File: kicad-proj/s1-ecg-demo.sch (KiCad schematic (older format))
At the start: 1 part

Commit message: added schematic
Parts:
- added C? (x2): 0.22u, symbol Device:C_Small
- added C? (x2): 0.1u, symbol Device:C_Small
- added C?: 1n, symbol Device:C_Small
- added C?: 22n, symbol Device:C_Small
- added C?: 11n, symbol Device:C_Small
- added D?: LED, symbol Device:LED
- added J?: USB-C-16-Pin, symbol s1-ecg-demo:USB-C-16-Pin
- added J?: Conn_ARM_JTAG_SWD_10, symbol Connector:Conn_ARM_JTAG_SWD_10
- added J?: Battery Port, symbol Connector_Generic:Conn_01x02
- added R? (x2): 5.1k, symbol Device:R_Small
- added R? (x2): 1M, symbol Device:R_Small
- added R? (x2): 100k, symbol Device:R_Small
- added R? (x6): 10M, symbol Device:R_Small
- added R? (x3): 150k, symbol Device:R_Small
- added R?: 665, symbol Device:R_Small
- added U?: AD8233, symbol s1-ecg-demo:AD8233
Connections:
- net GND: now reaches MOD?.1 (GND)
- net GND: now also MOD?.14 (GND), MOD?.20 (GND), C?.2, C?.2, D?.1 (K), J?.2 (Pin_2), J?.3 (GND), J?.5 (GND), J?.9 (GNDDetect), J?.A1/B12 (GND), J?.A12/B1 (GND), R?.1, R?.1, R?.2, U?.A1 (GND), U?.B3 (FR)
- net VBUS: now reaches MOD?.10 (Vcharge)
- net VBUS: now also J?.A4/B9 (VBUS), J?.A9/B4 (VBUS)
- net VBAT: now reaches MOD?.11 (Vbattery)
- net VBAT: now also J?.1 (Pin_1)
- net A3V3: now reaches MOD?.13 (Vio)
- net A3V3: now also C?.1, R?.2, U?.A2 (V+), U?.B1 (~SDN), U?.B2 (AC/~DC), U?.C2 (RLD_~SDN)
- net RA: now reaches MOD?.15 (A2)
- net RA: now also R?.1, R?.2
- net LA: now reaches MOD?.16 (A1)
- net LA: now also R?.1, R?.2
- net VREF: now reaches MOD?.17 (Vadc)
- net VREF: now also J?.1 (VTref)
- net SWDIO: now reaches MOD?.18 (SWDIO)
- net SWDIO: now also J?.2 (SWDIO/TMS)
- net SWDCLK: now reaches MOD?.19 (SWDCLK)
- net SWDCLK: now also J?.4 (SWDCLK/TCK)
- net D-: now reaches MOD?.2 (D2)
- net D-: now also J?.A7 (D-), J?.B7 (D-)
- net LED: now reaches MOD?.3 (D3)
- net LED: now also R?.2
- net LOD: now reaches MOD?.4 (D4)
- net LOD: now also U?.C1 (LOD)
- net D+: now reaches MOD?.5 (D1)
- net D+: now also J?.A6 (D+), J?.B6 (D+)
- new net: C?.1, R?.1, R?.1, U?.A3 (REFIN)
- new net: C?.2, R?.1, U?.A4 (HPSENSE)
- new net: C?.1, U?.A5 (HPDRIVE)
- new net: C?.2, R?.2, U?.B4 (IAOUT)
- new net: R?.1, U?.B5 (IN+)
- new net: C?.1, R?.1, R?.2, U?.C3 (REFOUT)
- new net: C?.2, R?.1, U?.C4 (RLDFB)
- new net: R?.1, U?.C5 (IN-)
- new net: R?.1, R?.2, U?.D2 (OPAMP-)
- new net: C?.2, R?.1, U?.D3 (OPMAMP+)
- new net: C?.1, R?.2, R?.2, R?.2, U?.D5 (RLD)
- new net: J?.A5 (CC1), R?.2
- new net: J?.B5 (CC2), R?.2
- new net: C?.1, R?.1, R?.1
- new net: C?.2, R?.2, R?.2
- new net: D?.2 (A), R?.1
- new net ECG_OUT: C?.1, R?.2, U?.D1 (OUT)
- no-connect marks 0 -> 7
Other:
- note added: "GAIN = 1100\n7Hz - 26Hz"
- moved on the sheet: MOD?

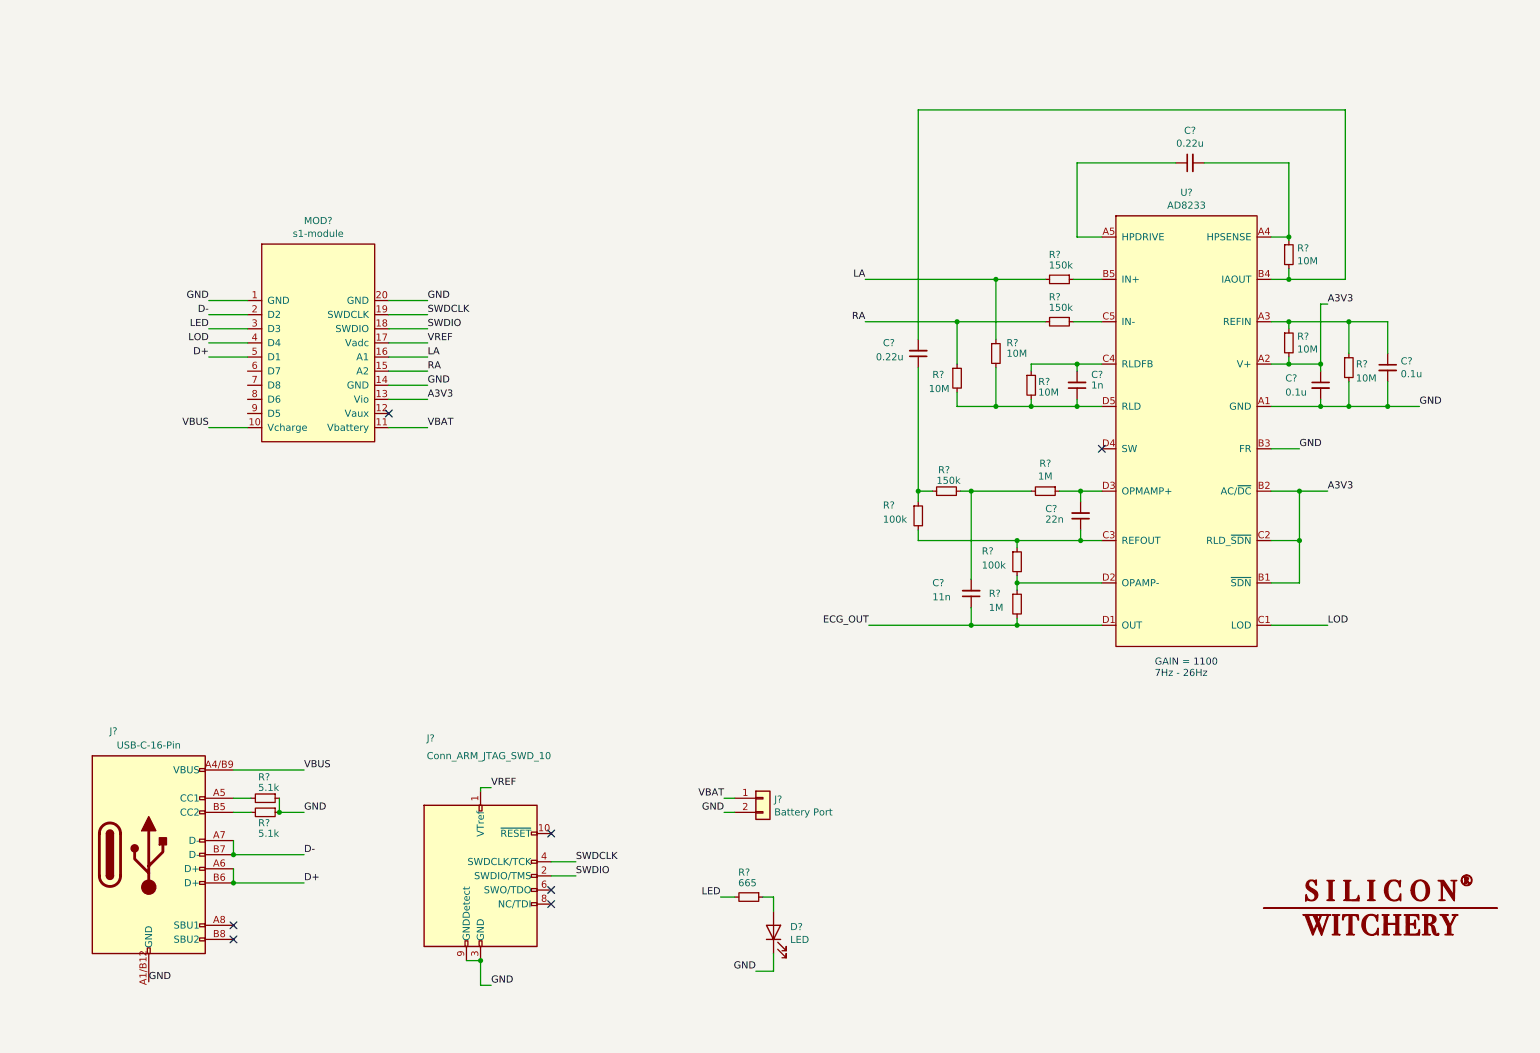
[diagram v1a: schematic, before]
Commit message: added BOM
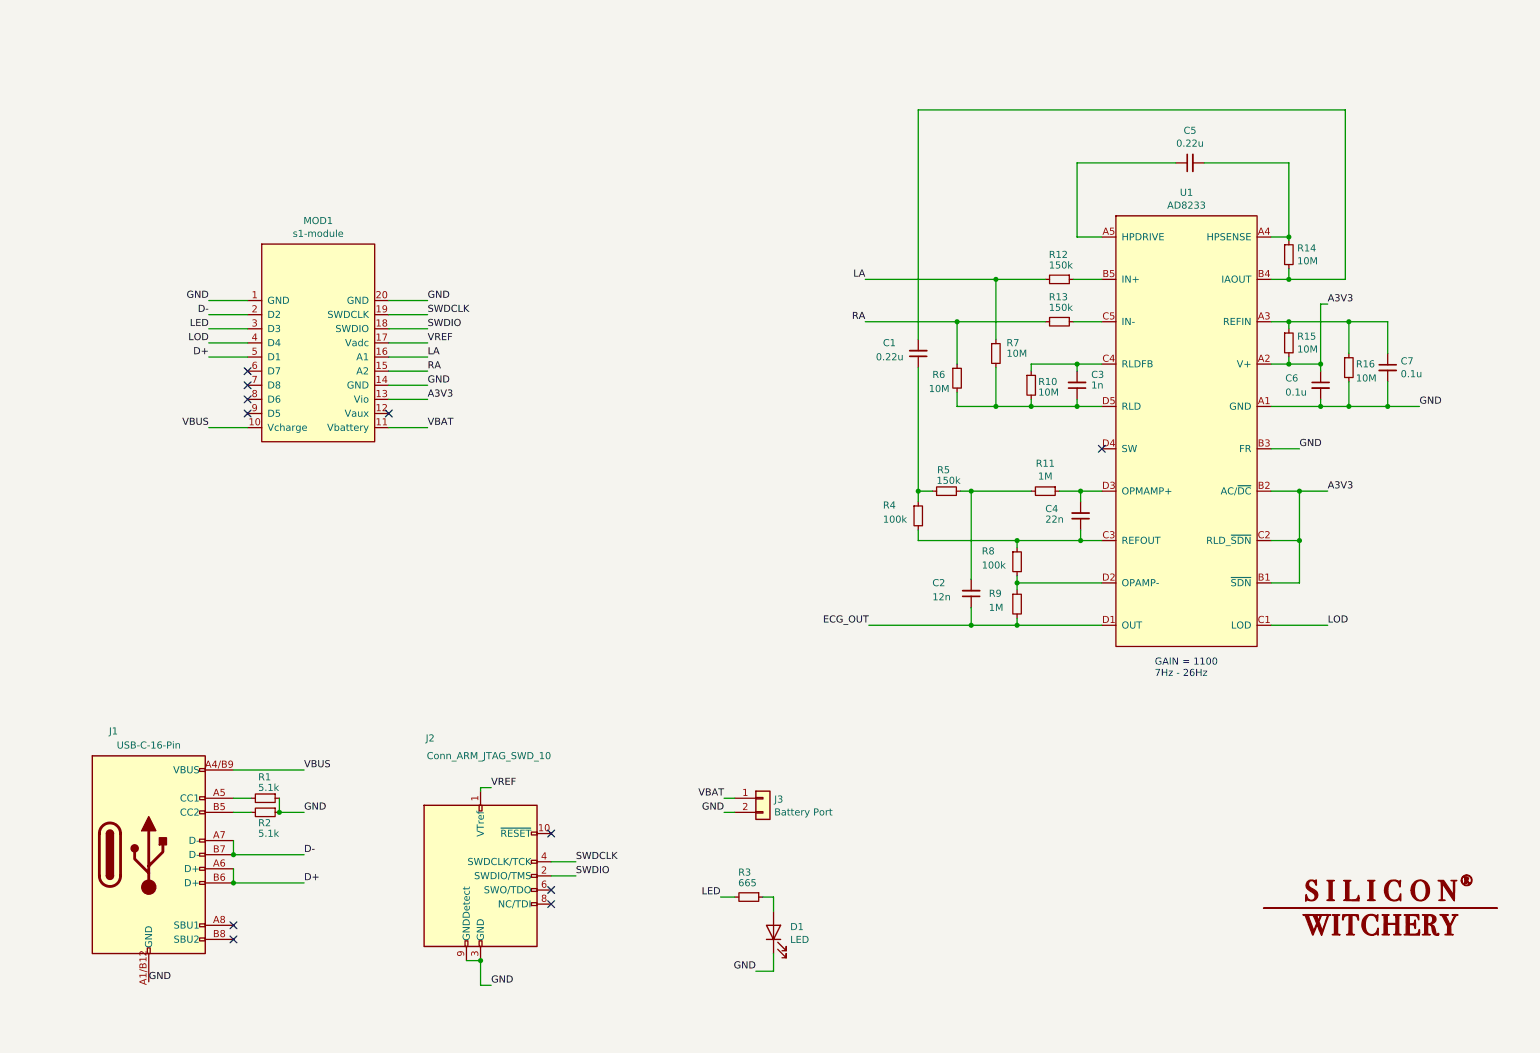
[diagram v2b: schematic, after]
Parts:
- C2: renamed from C?; value 11n -> 12n
- gave numbers to parts that had none: 28
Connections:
- no-connect marks 7 -> 11
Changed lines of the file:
@@
 $EndDescr
 $Comp
-L s1-module:s1-module MOD?
+L s1-module:s1-module MOD1
 U 1 1 61124856
 P 2675 3000
-F 0 "MOD?" H 2675 4015 50  0000 C CNN
+F 0 "MOD1" H 2675 4015 50  0000 C CNN
 F 1 "s1-module" H 2675 3924 50  0000 C CNN
 F 2 "s1-module:s1-module" H 2675 3900 50  0001 C CNN
@@
 $EndComp
 $Comp
-L sw-logo:LOGO #G?
+L sw-logo:LOGO #G1
 U 1 1 611251B7
 P 10200 6850
-F 0 "#G?" H 10200 6647 60  0001 C CNN
+F 0 "#G1" H 10200 6647 60  0001 C CNN
 F 1 "LOGO" H 10200 7053 60  0001 C CNN
 F 2 "" H 10200 6850 50  0001 C CNN
@@
 $EndComp
 $Comp
-L s1-ecg-demo:AD8233 U?
+L s1-ecg-demo:AD8233 U1
 U 1 1 6112908F
 P 8825 3450
-F 0 "U?" H 8825 5115 50  0000 C CNN
+F 0 "U1" H 8825 5115 50  0000 C CNN
 F 1 "AD8233" H 8825 5024 50  0000 C CNN
 F 2 "" H 7575 2950 50  0001 C CNN
@@
 $EndComp
 $Comp
-L Device:C_Small C?
+L Device:C_Small C5
 U 1 1 6112D102
 P 8850 1575
-F 0 "C?" V 9079 1575 50  0000 C CNN
+F 0 "C5" V 9079 1575 50  0000 C CNN
 F 1 "0.22u" V 8988 1575 50  0000 C CNN
 F 2 "" H 8850 1575 50  0001 C CNN
@@
 $EndComp
 $Comp
-L Device:C_Small C?
+L Device:C_Small C6
 U 1 1 6112DEAF
 P 9775 3150
-F 0 "C?" H 9525 3200 50  0000 L CNN
+F 0 "C6" H 9525 3200 50  0000 L CNN
 F 1 "0.1u" H 9525 3100 50  0000 L CNN
 F 2 "" H 9775 3150 50  0001 C CNN
@@
 $EndComp
 $Comp
-L Device:C_Small C?
+L Device:C_Small C7
 U 1 1 6112EC74
 P 10250 3025
-F 0 "C?" H 10342 3071 50  0000 L CNN
+F 0 "C7" H 10342 3071 50  0000 L CNN
 F 1 "0.1u" H 10342 2980 50  0000 L CNN
 F 2 "" H 10250 3025 50  0001 C CNN
@@
 $EndComp
 $Comp
-L Device:C_Small C?
+L Device:C_Small C3
 U 1 1 6113068D
 P 8050 3150
-F 0 "C?" H 7950 3075 50  0000 R CNN
+F 0 "C3" H 7950 3075 50  0000 R CNN
 F 1 "1n" H 7950 3150 50  0000 R CNN
 F 2 "" H 8050 3150 50  0001 C CNN
@@
 $EndComp
 $Comp
-L Device:C_Small C?
+L Device:C_Small C1
 U 1 1 6113493A
 P 6925 2925
-F 0 "C?" H 7175 2850 50  0000 R CNN
+F 0 "C1" H 7175 2850 50  0000 R CNN
 F 1 "0.22u" H 7225 2950 50  0000 R CNN
 F 2 "" H 6925 2925 50  0001 C CNN
@@
 $EndComp
 $Comp
-L Device:C_Small C?
+L Device:C_Small C4
 U 1 1 61136345
 P 8075 4075
-F 0 "C?" H 8325 4025 50  0000 R CNN
+F 0 "C4" H 8325 4025 50  0000 R CNN
 F 1 "22n" H 8325 4100 50  0000 R CNN
 F 2 "" H 8075 4075 50  0001 C CNN
@@
 $EndComp
 $Comp
-L Device:C_Small C?
+L Device:C_Small C2
 U 1 1 61137B1B
 P 7300 4625
-F 0 "C?" H 7575 4550 50  0000 R CNN
-F 1 "11n" H 7575 4650 50  0000 R CNN
+F 0 "C2" H 7575 4550 50  0000 R CNN
+F 1 "12n" H 7575 4650 50  0000 R CNN
 F 2 "" H 7300 4625 50  0001 C CNN
 F 3 "~" H 7300 4625 50  0001 C CNN
@@
 	7300 4525 7300 3900
 $Comp
-L Device:R_Small R?
+L Device:R_Small R9
 U 1 1 61146CE9
 P 7625 4700
-F 0 "R?" H 7425 4775 50  0000 L CNN
+F 0 "R9" H 7425 4775 50  0000 L CNN
 F 1 "1M" H 7425 4675 50  0000 L CNN
 F 2 "" H 7625 4700 50  0001 C CNN
@@
 $EndComp
 $Comp
-L Device:R_Small R?
+L Device:R_Small R8
 U 1 1 611482B4
 P 7625 4400
-F 0 "R?" H 7375 4475 50  0000 L CNN
+F 0 "R8" H 7375 4475 50  0000 L CNN
 F 1 "100k" H 7375 4375 50  0000 L CNN
 F 2 "" H 7625 4400 50  0001 C CNN
@@
 	8225 3900 8075 3900
 $Comp
-L Device:R_Small R?
+L Device:R_Small R11
 U 1 1 611542F5
 P 7825 3900
-F 0 "R?" V 7629 3900 50  0000 C CNN
+F 0 "R11" V 7629 3900 50  0000 C CNN
 F 1 "1M" V 7720 3900 50  0000 C CNN
 F 2 "" H 7825 3900 50  0001 C CNN
@@
 	8075 4250 7625 4250
 $Comp
-L Device:R_Small R?
+L Device:R_Small R15
 U 1 1 61157822
 P 9550 2850
-F 0 "R?" H 9609 2896 50  0000 L CNN
+F 0 "R15" H 9609 2896 50  0000 L CNN
 F 1 "10M" H 9609 2805 50  0000 L CNN
 F 2 "" H 9550 2850 50  0001 C CNN
@@
 	9550 2700 9975 2700
 $Comp
-L Device:R_Small R?
+L Device:R_Small R14
 U 1 1 6115B822
 P 9550 2225
-F 0 "R?" H 9609 2271 50  0000 L CNN
+F 0 "R14" H 9609 2271 50  0000 L CNN
 F 1 "10M" H 9609 2180 50  0000 L CNN
 F 2 "" H 9550 2225 50  0001 C CNN
@@
 Connection ~ 9550 2100
 $Comp
-L Device:R_Small R?
+L Device:R_Small R16
 U 1 1 61162002
 P 9975 3025
-F 0 "R?" H 10025 3050 50  0000 L CNN
+F 0 "R16" H 10025 3050 50  0000 L CNN
 F 1 "10M" H 10025 2950 50  0000 L CNN
 F 2 "" H 9975 3025 50  0001 C CNN
@@
 	9625 4250 9425 4250
 $Comp
-L Device:R_Small R?
+L Device:R_Small R10
 U 1 1 611962E1
 P 7725 3150
-F 0 "R?" H 7775 3175 50  0000 L CNN
+F 0 "R10" H 7775 3175 50  0000 L CNN
 F 1 "10M" H 7775 3100 50  0000 L CNN
 F 2 "" H 7725 3150 50  0001 C CNN
@@
 $EndComp
 $Comp
-L Device:R_Small R?
+L Device:R_Small R7
 U 1 1 61197DAA
 P 7475 2925
-F 0 "R?" H 7550 3000 50  0000 L CNN
+F 0 "R7" H 7550 3000 50  0000 L CNN
 F 1 "10M" H 7550 2925 50  0000 L CNN
 F 2 "" H 7475 2925 50  0001 C CNN
@@
 Connection ~ 7725 3300
 $Comp
-L Device:R_Small R?
+L Device:R_Small R6
 U 1 1 6119C8AC
 P 7200 3100
-F 0 "R?" H 7025 3125 50  0000 L CNN
+F 0 "R6" H 7025 3125 50  0000 L CNN
 F 1 "10M" H 7000 3025 50  0000 L CNN
 F 2 "" H 7200 3100 50  0001 C CNN
@@
 Connection ~ 7475 3300
 $Comp
-L Device:R_Small R?
+L Device:R_Small R12
 U 1 1 6119E901
 P 7925 2400
-F 0 "R?" V 7750 2325 50  0000 L CNN
+F 0 "R12" V 7750 2325 50  0000 L CNN
 F 1 "150k" V 7825 2325 50  0000 L CNN
 F 2 "" H 7925 2400 50  0001 C CNN
@@
 $EndComp
 $Comp
-L Device:R_Small R?
+L Device:R_Small R13
 U 1 1 6119FD58
 P 7925 2700
-F 0 "R?" V 7750 2625 50  0000 L CNN
+F 0 "R13" V 7750 2625 50  0000 L CNN
 F 1 "150k" V 7825 2625 50  0000 L CNN
 F 2 "" H 7925 2700 50  0001 C CNN
@@
 NoConn ~ 8225 3600
 $Comp
-L Device:R_Small R?
+L Device:R_Small R5
 U 1 1 611CE91D
 P 7125 3900
-F 0 "R?" V 7275 3875 50  0000 L CNN
+F 0 "R5" V 7275 3875 50  0000 L CNN
 F 1 "150k" V 7200 3800 50  0000 L CNN
 F 2 "" H 7125 3900 50  0001 C CNN
@@
 $EndComp
 $Comp
-L Device:R_Small R?
+L Device:R_Small R4
 U 1 1 611D1A4B
 P 6925 4075
-F 0 "R?" H 6675 4150 50  0000 L CNN
+F 0 "R4" H 6675 4150 50  0000 L CNN
 F 1 "100k" H 6675 4050 50  0000 L CNN
 F 2 "" H 6925 4075 50  0001 C CNN
@@
 GAIN = 1100\n7Hz - 26Hz
 $Comp
-L s1-ecg-demo:USB-C-16-Pin J?
+L s1-ecg-demo:USB-C-16-Pin J1
 U 1 1 6112F19C
 P 1475 6475
-F 0 "J?" H 1225 7350 50  0000 C CNN
+F 0 "J1" H 1225 7350 50  0000 C CNN
 F 1 "USB-C-16-Pin" H 1475 7250 50  0000 C CNN
 F 2 "" H 1475 6475 50  0001 C CNN
@@
 	2075 6575 2075 6675
 $Comp
-L Device:R_Small R?
+L Device:R_Small R1
 U 1 1 6113C090
 P 2300 6075
-F 0 "R?" V 2150 6025 50  0000 L CNN
+F 0 "R1" V 2150 6025 50  0000 L CNN
 F 1 "5.1k" V 2225 6025 50  0000 L CNN
 F 2 "" H 2300 6075 50  0001 C CNN
@@
 $EndComp
 $Comp
-L Device:R_Small R?
+L Device:R_Small R2
 U 1 1 6113DBC7
 P 2300 6175
-F 0 "R?" V 2375 6125 50  0000 L CNN
+F 0 "R2" V 2375 6125 50  0000 L CNN
 F 1 "5.1k" V 2450 6125 50  0000 L CNN
 F 2 "" H 2300 6175 50  0001 C CNN
@@
 GND
 $Comp
-L Connector:Conn_ARM_JTAG_SWD_10 J?
+L Connector:Conn_ARM_JTAG_SWD_10 J2
 U 1 1 61185655
 P 3825 6625
-F 0 "J?" H 3500 7600 50  0000 R CNN
+F 0 "J2" H 3500 7600 50  0000 R CNN
 F 1 "Conn_ARM_JTAG_SWD_10" H 4325 7475 50  0000 R CNN
 F 2 "" H 3825 6625 50  0001 C CNN
@@
 	4325 6625 4500 6625
 $Comp
-L Connector_Generic:Conn_01x02 J?
+L Connector_Generic:Conn_01x02 J3
 U 1 1 611DEDCA
 P 5825 6075
-F 0 "J?" H 5905 6067 50  0000 L CNN
+F 0 "J3" H 5905 6067 50  0000 L CNN
 F 1 "Battery Port" H 5905 5976 50  0000 L CNN
 F 2 "" H 5825 6075 50  0001 C CNN
@@
 	5550 6075 5625 6075
 $Comp
-L Device:LED D?
+L Device:LED D1
 U 1 1 611FA4FD
 P 5900 7025
-F 0 "D?" V 5939 6907 50  0000 R CNN
+F 0 "D1" V 5939 6907 50  0000 R CNN
 F 1 "LED" V 5848 6907 50  0000 R CNN
 F 2 "" H 5900 7025 50  0001 C CNN
@@
 $EndComp
 $Comp
-L Device:R_Small R?
+L Device:R_Small R3
 U 1 1 611FF2F6
 P 5725 6775
-F 0 "R?" V 5550 6700 50  0000 L CNN
+F 0 "R3" V 5550 6700 50  0000 L CNN
 F 1 "665" V 5625 6700 50  0000 L CNN
 F 2 "" H 5725 6775 50  0001 C CNN
@@
 Wire Wire Line
 	1900 2750 2175 2750
+NoConn ~ 2175 3050
+NoConn ~ 2175 3150
+NoConn ~ 2175 3250
+NoConn ~ 2175 3350
 $EndSCHEMATC

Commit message: Updated LEDs and BOM
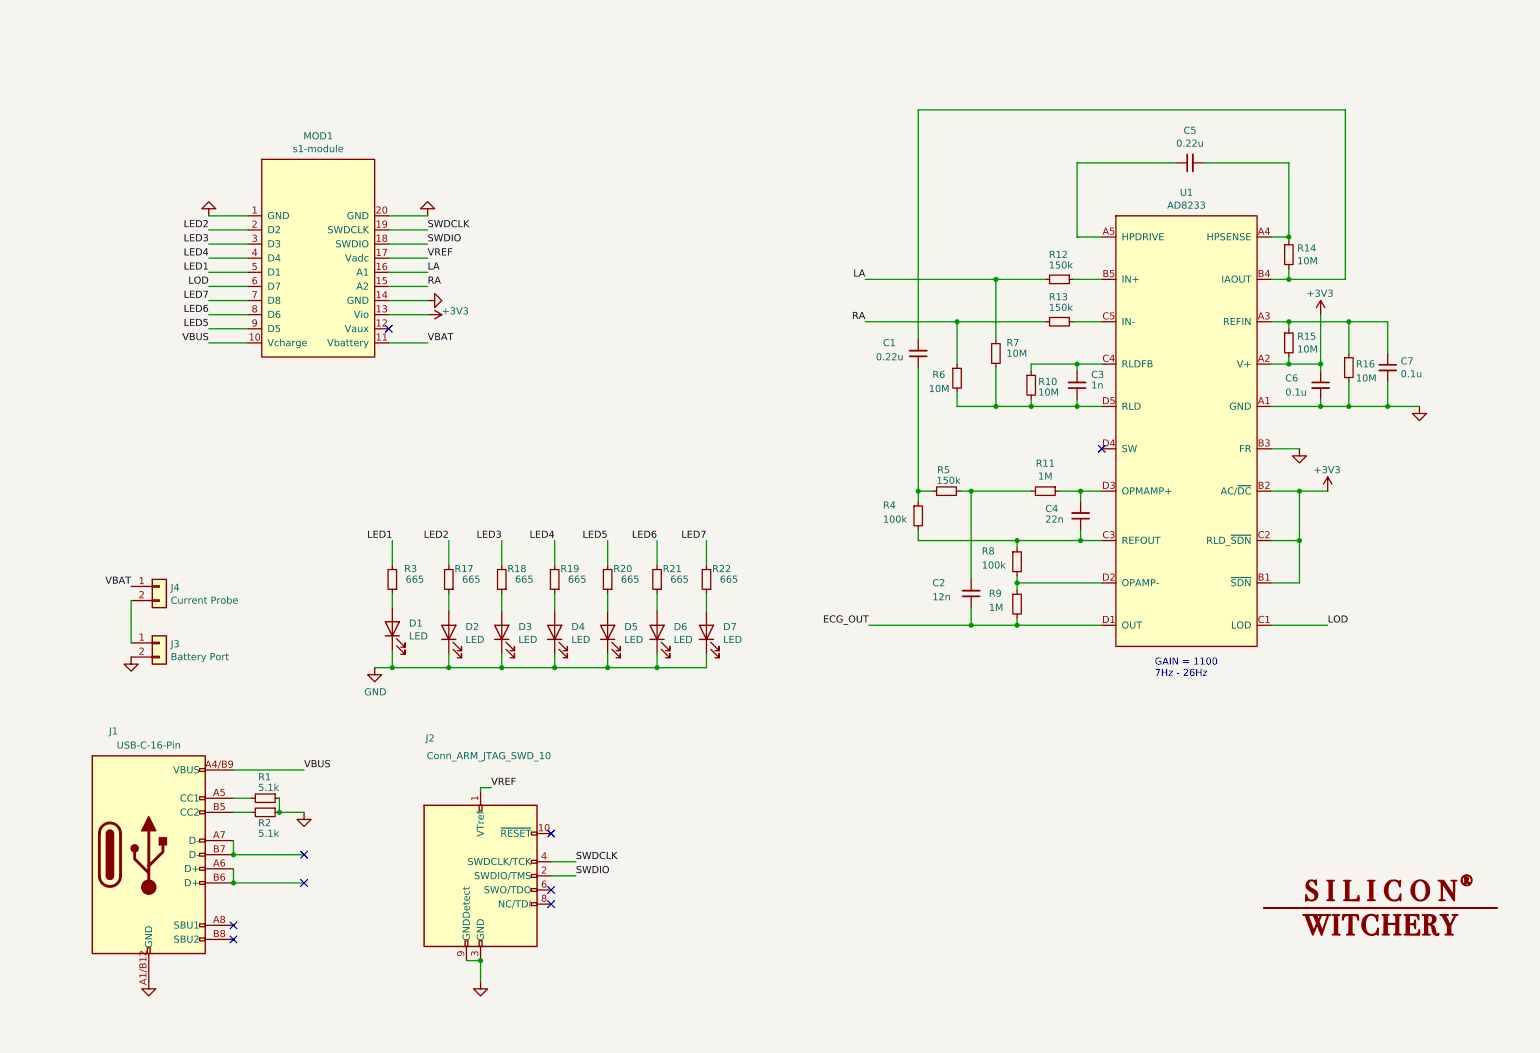
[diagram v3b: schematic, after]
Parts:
- added D2, D3, D4, D5, D6, D7: LED, symbol Device:LED
- added J4: Current Probe, symbol Connector_Generic:Conn_01x02
- added R17, R18, R19, R20, R21, R22: 665, symbol Device:R_Small
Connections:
- net GND: now also D2.1 (K), D3.1 (K), D4.1 (K), D5.1 (K), D6.1 (K), D7.1 (K)
- net LOD: now also MOD1.6 (D7); no longer MOD1.4 (D4)
- net VBAT: now also J4.1 (Pin_1); no longer J3.1 (Pin_1)
- net LED7: now reaches MOD1.7 (D8)
- net LED7: now also R22.2
- net LED6: now reaches MOD1.8 (D6)
- net LED6: now also R21.2
- net LED5: now reaches MOD1.9 (D5)
- net LED5: now also R20.2
- net A3V3 renamed +3V3
- net D+: no longer names the net of J1.A6 (D+), J1.B6 (D+)
- net D+: no longer MOD1.5 (D1)
- net D-: no longer names the net of J1.A7 (D-), J1.B7 (D-)
- net D-: no longer MOD1.2 (D2)
- net LED renamed LED1
- net LED1: now also MOD1.5 (D1); no longer MOD1.3 (D3)
- new net: D2.2 (A), R17.1
- new net: D3.2 (A), R18.1
- new net: D4.2 (A), R19.1
- new net: D5.2 (A), R20.1
- new net: D6.2 (A), R21.1
- new net: D7.2 (A), R22.1
- new net: J3.1 (Pin_1), J4.2 (Pin_2)
- new net LED2: MOD1.2 (D2), R17.2
- new net LED3: MOD1.3 (D3), R18.2
- new net LED4: MOD1.4 (D4), R19.2
- no-connect marks 11 -> 9
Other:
- moved on the sheet: D1, J3, MOD1, R3
